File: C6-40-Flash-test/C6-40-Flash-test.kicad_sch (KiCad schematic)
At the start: 23 parts, among them IC1 W25Q80DVSSIG, J1 USB_C_Receptacle_USB2.0, J2 Conn_01x07, J3 Conn_01x07, SW1 SW_Push_Dual, U1 SeeeduinoXIAO, U2 ESP32-C6, U3 MCP1700-3302E_SOT23, X1 Crystal 40 Mhz 10ppm

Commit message: Make antenna better (Is a shoelace)
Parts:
- added IC2: W25Q128JVSIQ, SOIC127P790X216-8N, symbol FLASH2:W25Q128JVSIQ
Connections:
- net GND: now also IC2.4 (GND)
- net SPICLK: now also IC2.6 (CLK)
- net SPICS0: now also IC2.1 (/CS)
- net SPIVDD: now also J3.4 (Pin_4), IC2.8 (VCC)
- net SPI_D0: now also IC2.5 (DI_(IO0))
- net SPI_D1: now also IC2.2 (DO_(IO1))
- net SPI_D2: now also IC2.3 (/WP_(IO2))
- net SPI_D3: now also IC2.7 (/HOLD_OR_/RESET_(IO3))
- net TX: now reaches U2.29 (U0TXD/GPIO16/FSPICS0)
- net TX: now also J3.6 (Pin_6)
- net RX: now reaches U2.30 (U0RXD/GPIO17/FSPICS1)
- net RX: now also J3.5 (Pin_5)
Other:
- note added: "Second Flash. On bottom side (OPTIONAL)"
- note added: "WARNING: Connecting 2 SPI flash chips at the same time can create a loop of ETHERNAL DEAD"

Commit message: C6 test new Flash
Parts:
- removed IC1: W25Q80DVSSIG, foot_main:SOIC127P790X216-8N-FLASH, symbol FLASH:W25Q80DVSSIG
- added IC1: AT25SF041-XMHD-T, footprints:SOP65P640X120-8N_flash, symbol FLASH:AT25SF041-XMHD-T
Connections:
- net GND: now also IC1.4 (GND)
- net SPICLK: now also IC1.6 (SCK)
- net SPICS0: now also IC1.1 (~{CS})
- net SPIVDD: now also IC1.8 (VCC)
- net SPI_D0: now also IC1.5 (SI)
- net SPI_D1: now also IC1.2 (SO)
- net SPI_D2: now also IC1.3 (~{WP})
- net SPI_D3: now also IC1.7 (~{HOLD})
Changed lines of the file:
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@@
     (stroke (width 0) (type default))
   )
-  (wire (pts (xy 280.67 162.56) (xy 290.83 162.56))
+  (wire (pts (xy 280.67 162.56) (xy 298.45 162.56))
     (stroke (width 0) (type default))
   )
@@
     (stroke (width 0) (type default))
   )
+  (wire (pts (xy 326.39 160.02) (xy 342.9 160.02))
+    (stroke (width 0) (type default))
+  )
   (wire (pts (xy 215.9 106.68) (xy 215.9 102.87))
     (stroke (width 0) (type default))
@@
     (stroke (width 0) (type default))
   )
+  (wire (pts (xy 326.39 167.64) (xy 334.01 167.64))
+    (stroke (width 0) (type default))
+  )
   (wire (pts (xy 240.03 167.64) (xy 240.03 166.37))
     (stroke (width 0) (type default))
   )
-  (wire (pts (xy 342.9 165.1) (xy 334.01 165.1))
+  (wire (pts (xy 326.39 165.1) (xy 342.9 165.1))
     (stroke (width 0) (type default))
   )
@@
     (stroke (width 0) (type default))
   )
+  (wire (pts (xy 290.83 167.64) (xy 298.45 167.64))
+    (stroke (width 0) (type default))
+  )
   (wire (pts (xy 255.27 57.15) (xy 252.73 57.15))
     (stroke (width 0) (type default))
@@
     (stroke (width 0) (type default))
   )
+  (wire (pts (xy 290.83 165.1) (xy 298.45 165.1))
+    (stroke (width 0) (type default))
+  )
   (polyline (pts (xy 138.43 191.77) (xy 203.2 191.77))
     (stroke (width 0) (type default))
@@
     (stroke (width 0) (type default))
   )
-  (wire (pts (xy 334.01 160.02) (xy 342.9 160.02))
+  (wire (pts (xy 326.39 162.56) (xy 334.01 162.56))
     (stroke (width 0) (type default))
   )
@@
   )
   (wire (pts (xy 215.9 74.93) (xy 215.9 76.2))
+    (stroke (width 0) (type default))
+  )
+  (wire (pts (xy 290.83 160.02) (xy 298.45 160.02))
     (stroke (width 0) (type default))
   )
@@
         (path "/b44a77cd-78b0-458d-a6b9-91ee99b52f9e"
           (reference "#PWR023") (unit 1)
+        )
+      )
+    )
+  )
+  (symbol (lib_id "FLASH:AT25SF041-XMHD-T") (at 298.45 160.02 0) (unit 1)
+    (in_bom yes) (on_board yes) (dnp no) (fields_autoplaced)
+    (property "Reference" "IC1" (at 312.42 153.3357 0)
+      (effects (font (size 1.27 1.27)))
+    )
+    (property "Value" "AT25SF041-XMHD-T" (at 312.42 155.7599 0)
+      (effects (font (size 1.27 1.27)))
+    )
+    (property "Footprint" "footprints:SOP65P640X120-8N_flash" (at 322.58 254.94 0)
+      (effects (font (size 1.27 1.27)) (justify left top) hide)
+    )
+    (property "Datasheet" "http://www.mouser.com/datasheet/2/590/DS-AT25SF041_044-1385758.pdf" (at 322.58 354.94 0)
+      (effects (font (size 1.27 1.27)) (justify left top) hide)
+    )
+    (property "Height" "1.2" (at 322.58 554.94 0)
+      (effects (font (size 1.27 1.27)) (justify left top) hide)
+    )
+    (property "Manufacturer_Name" "Adesto Technologies" (at 322.58 654.94 0)
+      (effects (font (size 1.27 1.27)) (justify left top) hide)
+    )
+    (property "Manufacturer_Part_Number" "AT25SF041-XMHD-T" (at 322.58 754.94 0)
+      (effects (font (size 1.27 1.27)) (justify left top) hide)
+    )
+    (property "Mouser Part Number" "988-AT25SF041-XMHD-T" (at 322.58 854.94 0)
+      (effects (font (size 1.27 1.27)) (justify left top) hide)
+    )
+    (property "Mouser Price/Stock" "https://www.mouser.co.uk/ProductDetail/Adesto-Technologies/AT25SF041-XMHD-T?qs=egr8I6xqk3vEJVfEli6XrA%3D%3D" (at 322.58 954.94 0)
+      (effects (font (size 1.27 1.27)) (justify left top) hide)
+    )
+    (property "Arrow Part Number" "AT25SF041-XMHD-T" (at 322.58 1054.94 0)
+      (effects (font (size 1.27 1.27)) (justify left top) hide)
+    )
+    (property "Arrow Price/Stock" "https://www.arrow.com/en/products/at25sf041-xmhd-t/adesto-technologies-corporation-inc" (at 322.58 1154.94 0)
+      (effects (font (size 1.27 1.27)) (justify left top) hide)
+    )
+    (pin "5")
+    (pin "1")
+    (pin "3")
+    (pin "6")
+    (pin "2")
+    (pin "7")
+    (pin "8")
+    (pin "4")
+    (instances
+      (project "C6-40-Flash-test"
+        (path "/b44a77cd-78b0-458d-a6b9-91ee99b52f9e"
+          (reference "IC1") (unit 1)
         )
       )
@@
         )
       )
-    )
-  )
-  (symbol (lib_id "FLASH:W25Q80DVSSIG") (at 290.83 160.02 0) (unit 1)
-    (in_bom yes) (on_board yes) (dnp no) (fields_autoplaced)
-    (property "Reference" "IC1" (at 312.42 153.3357 0)
-      (effects (font (size 1.27 1.27)))
-    )
-    (property "Value" "W25Q80DVSSIG" (at 312.42 155.7599 0)
-      (effects (font (size 1.27 1.27)))
-    )
-    (property "Footprint" "foot_main:SOIC127P790X216-8N-FLASH" (at 330.2 254.94 0)
-      (effects (font (size 1.27 1.27)) (justify left top) hide)
-    )
-    (property "Datasheet" "https://www.winbond.com/hq/search-resource-file.jsp?partNo=W25Q80DVSSIG&type=datasheet" (at 330.2 354.94 0)
-      (effects (font (size 1.27 1.27)) (justify left top) hide)
-    )
-    (property "Height" "2.16" (at 330.2 554.94 0)
-      (effects (font (size 1.27 1.27)) (justify left top) hide)
-    )
-    (property "Manufacturer_Name" "Winbond" (at 330.2 654.94 0)
-      (effects (font (size 1.27 1.27)) (justify left top) hide)
-    )
-    (property "Manufacturer_Part_Number" "W25Q80DVSSIG" (at 330.2 754.94 0)
-      (effects (font (size 1.27 1.27)) (justify left top) hide)
-    )
-    (property "Mouser Part Number" "454-W25Q80DVSSIG" (at 330.2 854.94 0)
-      (effects (font (size 1.27 1.27)) (justify left top) hide)
-    )
-    (property "Mouser Price/Stock" "https://www.mouser.co.uk/ProductDetail/Winbond/W25Q80DVSSIG?qs=qSfuJ%252Bfl%2Fd6z%2FQYNv5lpMA%3D%3D" (at 330.2 954.94 0)
-      (effects (font (size 1.27 1.27)) (justify left top) hide)
-    )
-    (property "Arrow Part Number" "W25Q80DVSSIG" (at 330.2 1054.94 0)
-      (effects (font (size 1.27 1.27)) (justify left top) hide)
-    )
-    (property "Arrow Price/Stock" "https://www.arrow.com/en/products/w25q80dvssig/winbond-electronics?region=nac" (at 330.2 1154.94 0)
-      (effects (font (size 1.27 1.27)) (justify left top) hide)
-    )
-    (pin "8")
-    (pin "4")
-    (pin "6")
-    (pin "1")
-    (pin "7")
-    (pin "2")
-    (pin "5")
-    (pin "3")
-    (instances
-      (project "C6-40-Flash-test"
-        (path "/b44a77cd-78b0-458d-a6b9-91ee99b52f9e"
-          (reference "IC1") (unit 1)
-        )
-      )

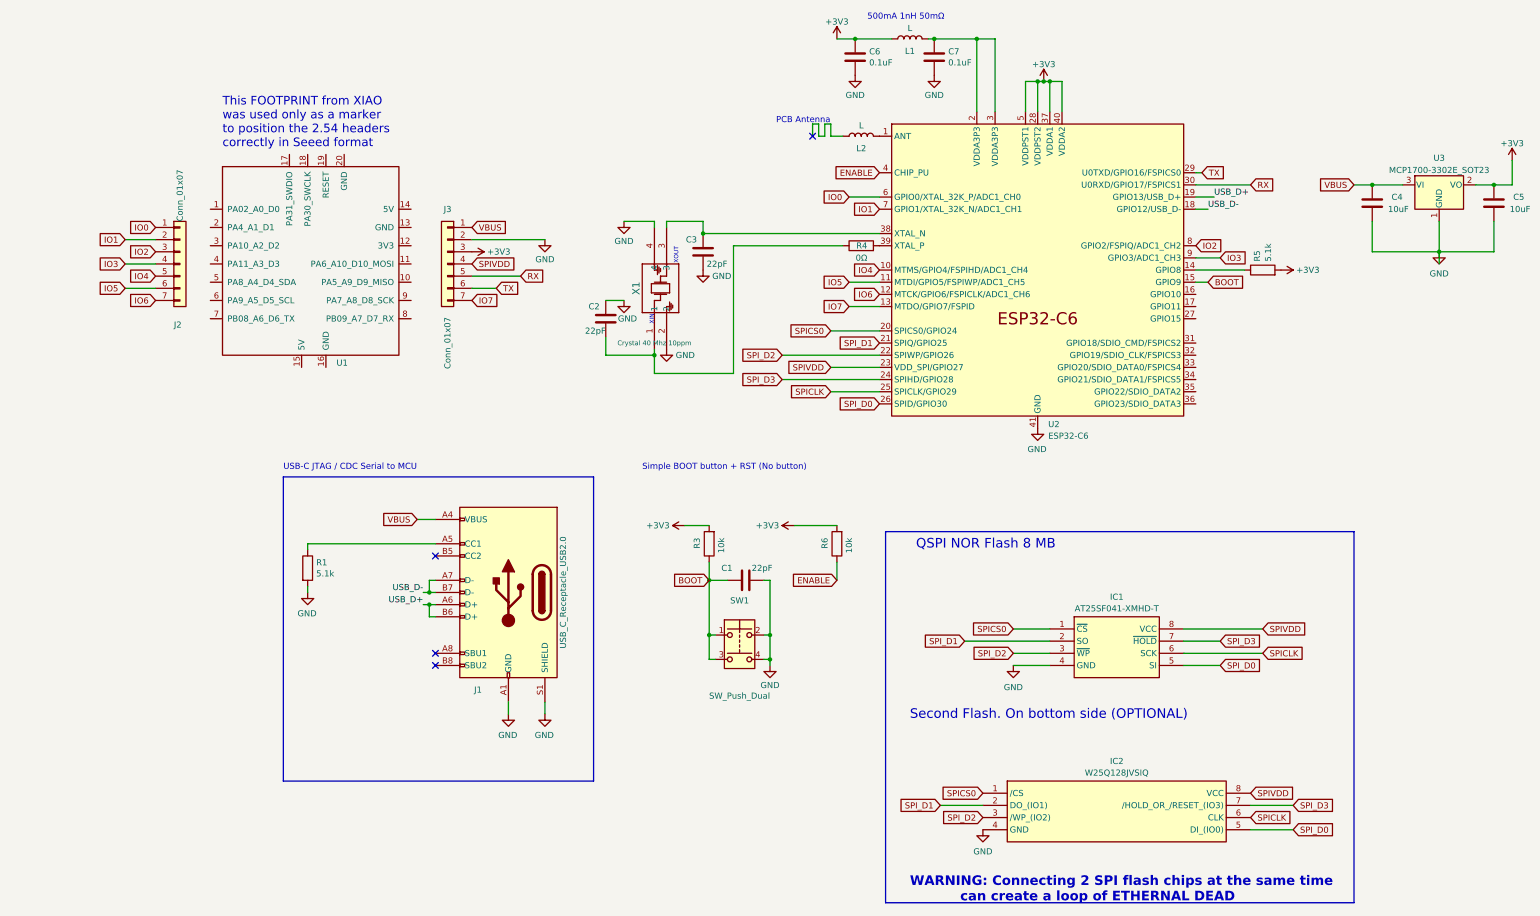
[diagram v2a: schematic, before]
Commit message: Test with external flash
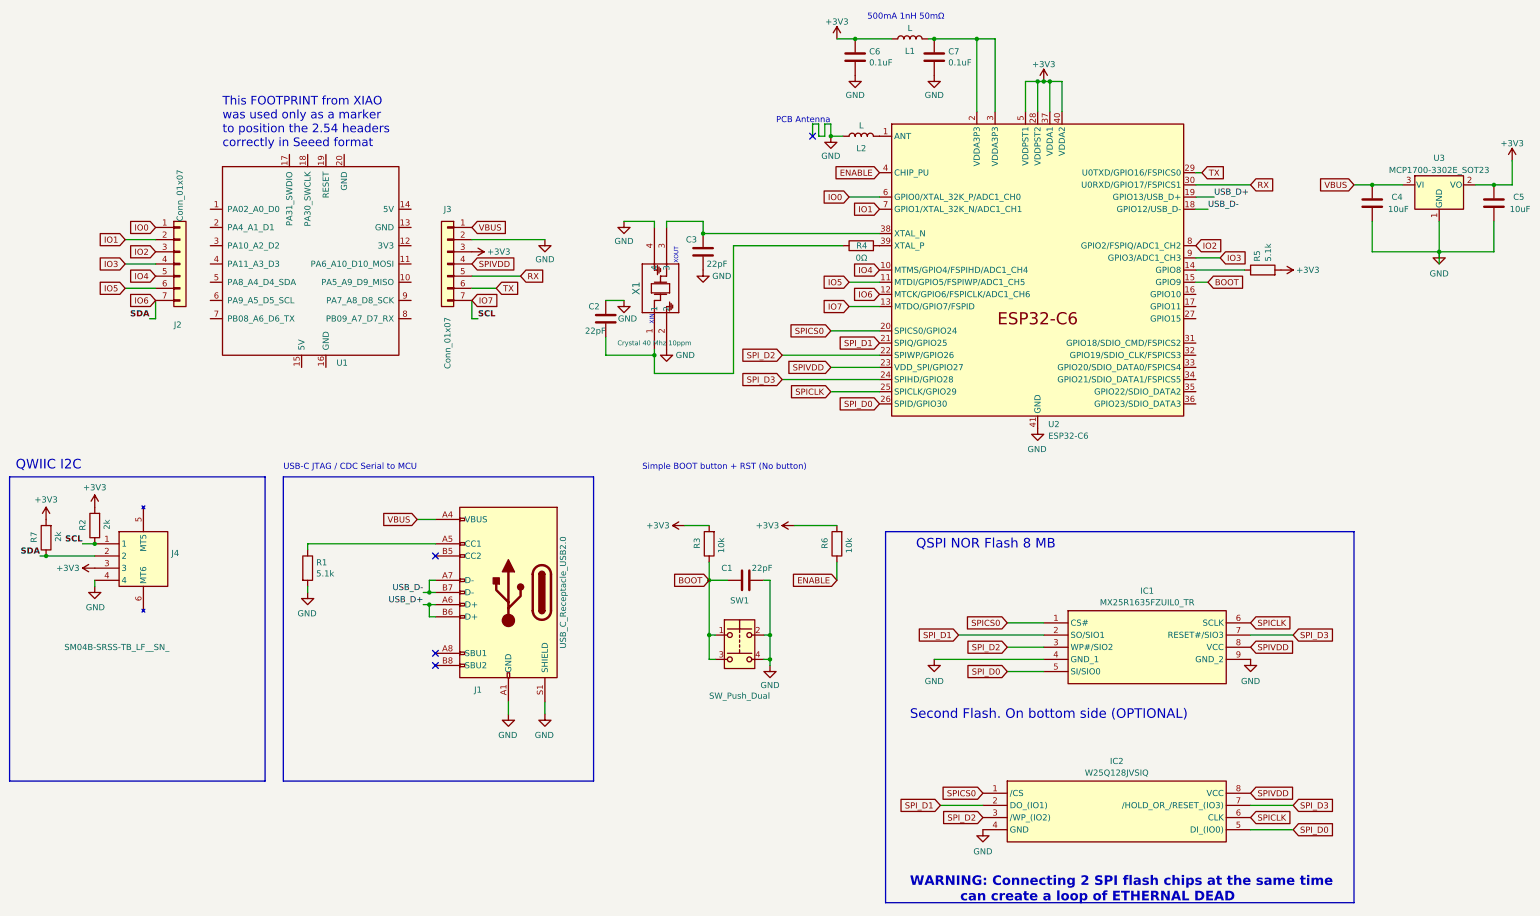
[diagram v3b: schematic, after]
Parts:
- removed IC1: AT25SF041-XMHD-T, footprints:SOP65P640X120-8N_flash, symbol FLASH:AT25SF041-XMHD-T
- added IC1: MX25R1635FZUIL0_TR, footprints:MX25R1635FZUIL0TR, symbol FLASH:MX25R1635FZUIL0_TR
- added J4: SM04B-SRSS-TB_LF__SN_, foot_main:QWIIC_SM04B-SRSS-TB_LFSN_, symbol QWIIC:SM04B-SRSS-TB_LF__SN_
- added R2, R7: 2k, Resistor_SMD:R_0402_1005Metric, symbol Device:R
- U2: LCSC (none) -> C5364646
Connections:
- net +3V3: now also J4.3, R2.2, R7.2
- net GND: now also L2.1, IC1.4 (GND_1), IC1.9 (GND_2), J4.4
- net IO6: now also J4.2, R7.1
- net IO7: now also J4.1, R2.1
- net SPICLK: now also IC1.6 (SCLK)
- net SPICS0: now also IC1.1 (CS#)
- net SPIVDD: now also IC1.8 (VCC)
- net SPI_D0: now also IC1.5 (SI/SIO0)
- net SPI_D1: now also IC1.2 (SO/SIO1)
- net SPI_D2: now also IC1.3 (WP#/SIO2)
- net SPI_D3: now also IC1.7 (RESET#/SIO3)
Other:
- note added: "QWIIC I2C"
